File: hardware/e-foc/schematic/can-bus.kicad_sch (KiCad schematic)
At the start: 10 parts

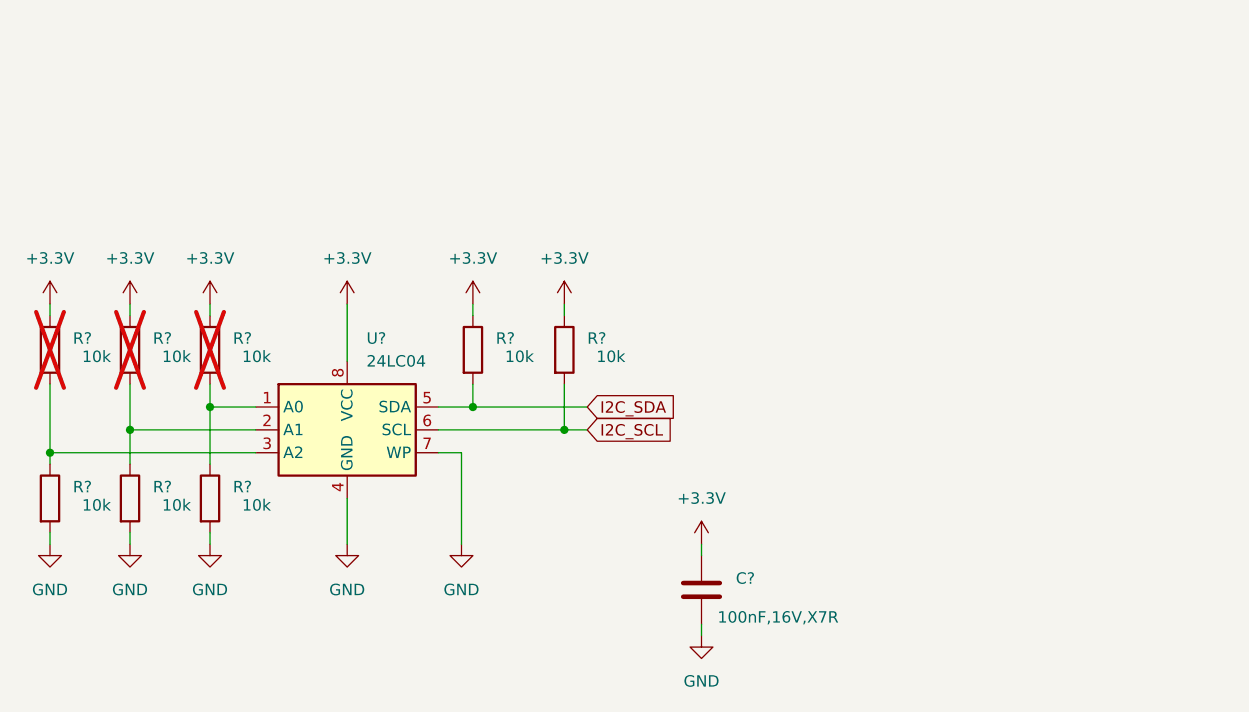
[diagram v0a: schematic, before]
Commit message: chore: add release please action (#1)
* add release please action

* refactor structure

* schematic finished

* pcb improvements

* board finished

* updates

* updates

* .\.claude\

* updates

* reorganize project

* fix ci

* fix ci

* fix(ci): disable kicad-bot bom/diff (not implemented in v0.1.3)

verify (ERC/DRC) passes, but run-bom-check and run-diff exit 2 with
"not available in this build yet (Phase 2/3)". Keep run-verify only.

Co-Authored-By: Claude Opus 4.8 <noreply@anthropic.com>

* feat(ci): visual schematic/PCB diff on pull requests

kicad-bot's diff phase isn't available in v0.1.x, so render PR head vs base
with kicad-cli and produce a red/green overlay (added/removed) per board via
Pillow — no KiAuto/GUI automation. New scripts/visual_diff.py + a matrix
kicad-diff.yml that uploads the diff images as a per-board artifact.

Co-Authored-By: Claude Opus 4.8 <noreply@anthropic.com>

* fix(erc): ignore power_pin_not_driven instead of per-instance exclusions

Both boards are powered through a connector, so power_pin_not_driven is an
expected false-positive. It was suppressed via GUI per-instance exclusions
(hashed by coordinates/UUIDs), which don't survive a different KiCad patch or
the PR merge commit in CI -> the violations resurfaced as ERC errors and
failed verify (e.g. tiva: 4 errors). Set the rule severity to "ignore" in
each .kicad_pro: deterministic, committed, version-independent. 0 ERC errors
on both boards now.

Co-Authored-By: Claude Opus 4.8 <noreply@anthropic.com>

---------

Co-authored-by: Claude Opus 4.8 <noreply@anthropic.com>
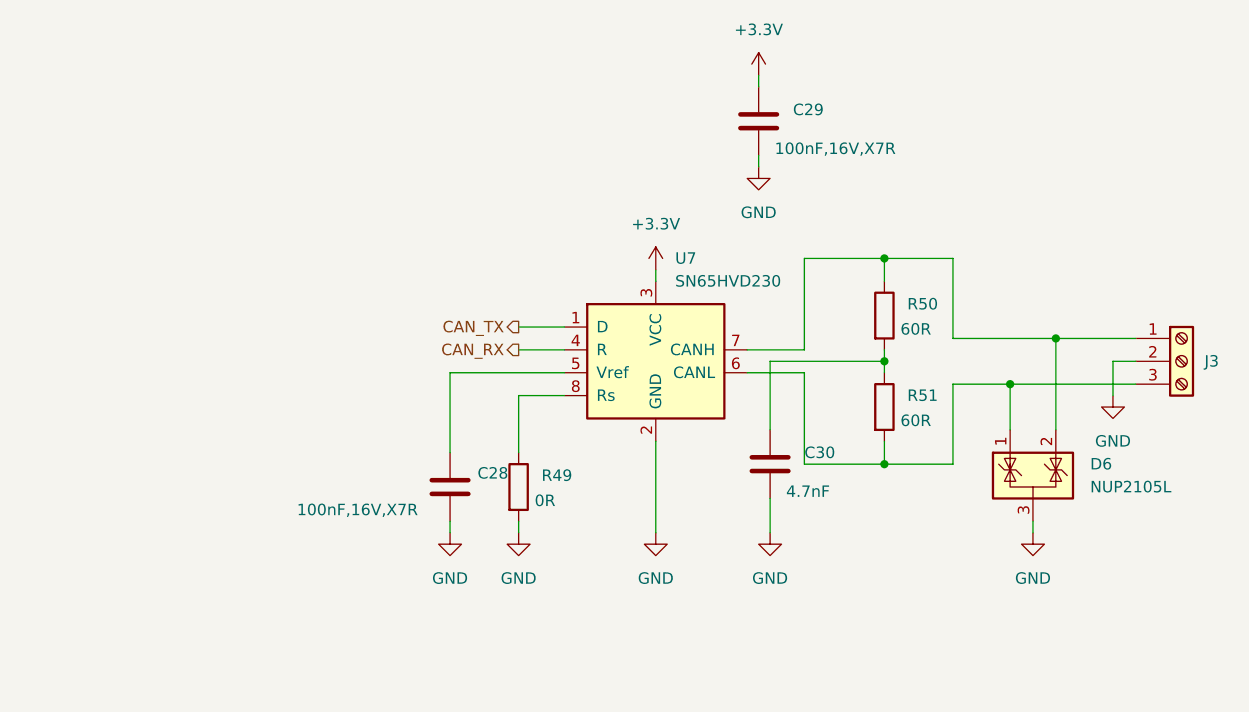
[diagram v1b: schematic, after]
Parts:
- removed C?: 100nF,16V,X7R, symbol Device:C
- removed R? (x8): 10k, Resistor_SMD:R_0805_2012Metric_Pad1.20x1.40mm_HandSolder, symbol Device:R
- removed U?: 24LC04, Package_SO:SOIC-8_3.9x4.9mm_P1.27mm, symbol Memory_EEPROM:24LC04
- added C28, C29: 100nF,16V,X7R, Capacitor_SMD:C_0805_2012Metric_Pad1.18x1.45mm_HandSolder, symbol Device:C
- added C30: 4.7nF, Capacitor_SMD:C_0805_2012Metric_Pad1.18x1.45mm_HandSolder, symbol Device:C
- added D6: NUP2105L, Package_TO_SOT_SMD:SOT-23W_Handsoldering, symbol Power_Protection:NUP2105L
- added J3: Screw_Terminal_01x03, TerminalBlock:TerminalBlock_Xinya_XY308-2.54-3P_1x03_P2.54mm_Horizontal, symbol Connector:Screw_Terminal_01x03
- added R49: 0R, Resistor_SMD:R_0805_2012Metric_Pad1.20x1.40mm_HandSolder, symbol Device:R
- added R50, R51: 60R, Resistor_SMD:R_0805_2012Metric_Pad1.20x1.40mm_HandSolder, symbol Device:R
- added U7: SN65HVD230, Package_SO:SOIC-8_3.9x4.9mm_P1.27mm, symbol Interface_CAN_LIN:SN65HVD230
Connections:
- net +3.3V: now also C29.1, U7.3 (VCC)
- net GND: now also C28.2, C29.2, C30.2, D6.3 (A), J3.2 (Pin_2), R49.2, U7.2 (GND)
- new net: D6.2 (K), J3.1 (Pin_1), R50.1, U7.7 (CANH)
- new net: D6.1 (K), J3.3 (Pin_3), R51.2, U7.6 (CANL)
- new net: R49.1, U7.8 (Rs)
- new net: C30.1, R50.2, R51.1
- new net: C28.1, U7.5 (Vref)
- new net CAN_RX: U7.4 (R)
- new net CAN_TX: U7.1 (D)
